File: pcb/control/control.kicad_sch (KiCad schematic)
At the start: 2 parts, among them U1 PicoW, U2 SN65HVD230DR

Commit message: Working on control PCB more
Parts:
- added C1: 4.7uF, symbol Device:C
- added C2: 10uF, symbol Device:C
- added C3: 100nF, symbol Device:C
- added CR1: PESD1CAN_215, pesd:SOT23_PESD1_NEX, symbol pesd:PESD1CAN_215
- added J1: Barrel_Jack_MountingPin, Connector_BarrelJack:BarrelJack_CUI_PJ-102AH_Horizontal, symbol Connector:Barrel_Jack_MountingPin
- added R1, R2: 60Ω, symbol Device:R
- added R3: R, symbol Device:R
- added R4: 100KΩ, symbol Device:R
- added R5, R6, R7: PTA4543, POT_PTA4543, symbol pta4543:PTA4543-2015DPA103
- added U3: FDN340P, fdn340p:SOT-23_ONS, symbol fdn340p:FDN340P
- added U4: DMG2305UX-7, SOT-23_DIO, symbol dmg2305ux:DMG2305UX-7
- U1: footprint RPi_PicoW:RPi_Pico_SMD_TH -> pico:RPi_PicoW_SMD_TH
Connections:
- net GND: now reaches U1.13 (GND)
- net GND: now also U1.18 (GND), U1.23 (GND), U1.28 (GND), U1.3 (GND), U1.33 (AGND), U1.38 (GND), U1.42 (GND), U1.8 (GND), U2.2 (GND), C1.2, C2.2, C3.2, CR1.3, J1.2, R3.2, R5.3, R6.3, R7.3
- net LED_ON: now reaches U1.14 (GPIO10)
- net LED_R: now reaches U1.15 (GPIO11)
- net LED_G: now reaches U1.16 (GPIO12)
- net LED_B: now reaches U1.19 (GPIO14)
- net LED_WIFI: now reaches U1.20 (GPIO15)
- net CAN_TX: now reaches U1.21 (GPIO16)
- net CAN_TX: now also U2.1 (D)
- net CAN_RX: now reaches U1.22 (GPIO17)
- net CAN_RX: now also U2.4 (R)
- net CAN_ENL: now reaches U1.29 (GPIO22)
- net CAN_ENL: now also R4.2, U3.1
- net POT_R: now reaches U1.31 (GPIO26_ADC0)
- net POT_R: now also R5.2
- net POT_G: now reaches U1.32 (GPIO27_ADC1)
- net POT_G: now also R6.2
- net POT_B: now reaches U1.34 (GPIO28_ADC2)
- net POT_B: now also R7.2
- net VSYS: now reaches U1.39 (VSYS)
- net VSYS: now also U2.3 (VCC), C2.1, C3.1, R4.1, R5.1, R6.1, R7.1, U3.2, U4.2
- net VBUS: now reaches U1.40 (VBUS)
- net VBUS: now also U4.1
- net CAN_VREF: now reaches U2.5 (VREF)
- net CAN_VREF: now also C1.1, R1.2, R2.1
- net CANL: now reaches U2.6 (CANL)
- net CANL: now also CR1.2, R2.2
- net CANH: now reaches U2.7 (CANH)
- net CANH: now also CR1.1, R1.1
- net CAN_RS: now reaches U2.8 (RS)
- net CAN_RS: now also R3.1, U3.3
- new net VBARREL: J1.1, U4.3
- no-connect marks 0 -> 20
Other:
- note added: "5V Supply"
- note added: "CAN Transceiver"
- note added: "Color Sliders"
- note added: "ESD Protection"
- note added: "Enable Logic"
- note added: "Microcontroller"
- note added: "Power"
- note added: "Split Termination"
- moved on the sheet: U1, U2

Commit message: Schematic finished, working on layout
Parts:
- added D1, D2, D3, D4, D5: LED, LED_THT:LED_D5.0mm, symbol Device:LED
- added J2: Screw_Terminal_01x02, TerminalBlock_TE-Connectivity:TerminalBlock_TE_282834-2_1x02_P2.54mm_Horizontal, symbol Connector:Screw_Terminal_01x02
- added R10, R11, R8, R9: 60Ω, Resistor_SMD:R_1206_3216Metric, symbol Device:R
- added R12: 5Ω, Resistor_SMD:R_0603_1608Metric, symbol Device:R
- added S1: RM103772BCB, rm103772bcb:RM103772BCB, symbol rm103772bcb:RM103772BCB
- added SW1, SW2: OS102011MS2QN1, os102011ms2qn1:SPDT_OS102011_CNK, symbol os102011ms2qn1:OS102011MS2QN1
- C1, C2, C3: footprint (none) -> Capacitor_SMD:C_0603_1608Metric
- R1, R2: footprint (none) -> Resistor_SMD:R_1206_3216Metric
- R3: value R -> 10KΩ; footprint (none) -> Resistor_SMD:R_0603_1608Metric
- R4: footprint (none) -> Resistor_SMD:R_0603_1608Metric
- U4: footprint SOT-23_DIO -> dmg2305ux:SOT-23_DIO
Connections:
- net CANH: now also J2.1 (Pin_1)
- net CANL: now also J2.2 (Pin_2)
- net GND: now also R10.2, R11.2, R12.2, R8.2, R9.2, SW1.3, SW2.3
- net LED_B: now also D5.2 (A)
- net LED_G: now also D4.2 (A)
- net LED_ON: now also D1.2 (A)
- net LED_R: now also D3.2 (A)
- net LED_WIFI: now also D2.2 (A)
- net VSYS: now also S1.8 (C), SW1.1, SW2.1
- net M_LIGHT: now reaches U1.10 (GPIO7)
- net M_LIGHT: now also S1.1
- net M_MUSIC: now reaches U1.11 (GPIO8)
- net M_MUSIC: now also S1.2
- net M_ON: now reaches U1.12 (GPIO9)
- net M_ON: now also S1.3
- net SYS_EN: now reaches U1.6 (GPIO4)
- net SYS_EN: now also SW1.2
- net SYS_WIFI: now reaches U1.7 (GPIO5)
- net SYS_WIFI: now also SW2.2
- new net: D1.1 (K), R8.1
- new net: D4.1 (K), R11.1
- new net: D5.1 (K), R12.1
- new net: D3.1 (K), R10.1
- new net: D2.1 (K), R9.1
- no-connect marks 20 -> 21
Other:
- note added: "B"
- note added: "Enable"
- note added: "G"
- note added: "LEDs"
- note added: "Mode"
- note added: "On"
- note added: "R"
- note added: "Screw Terminal"
- note added: "Switches"
- note added: "WiFi"

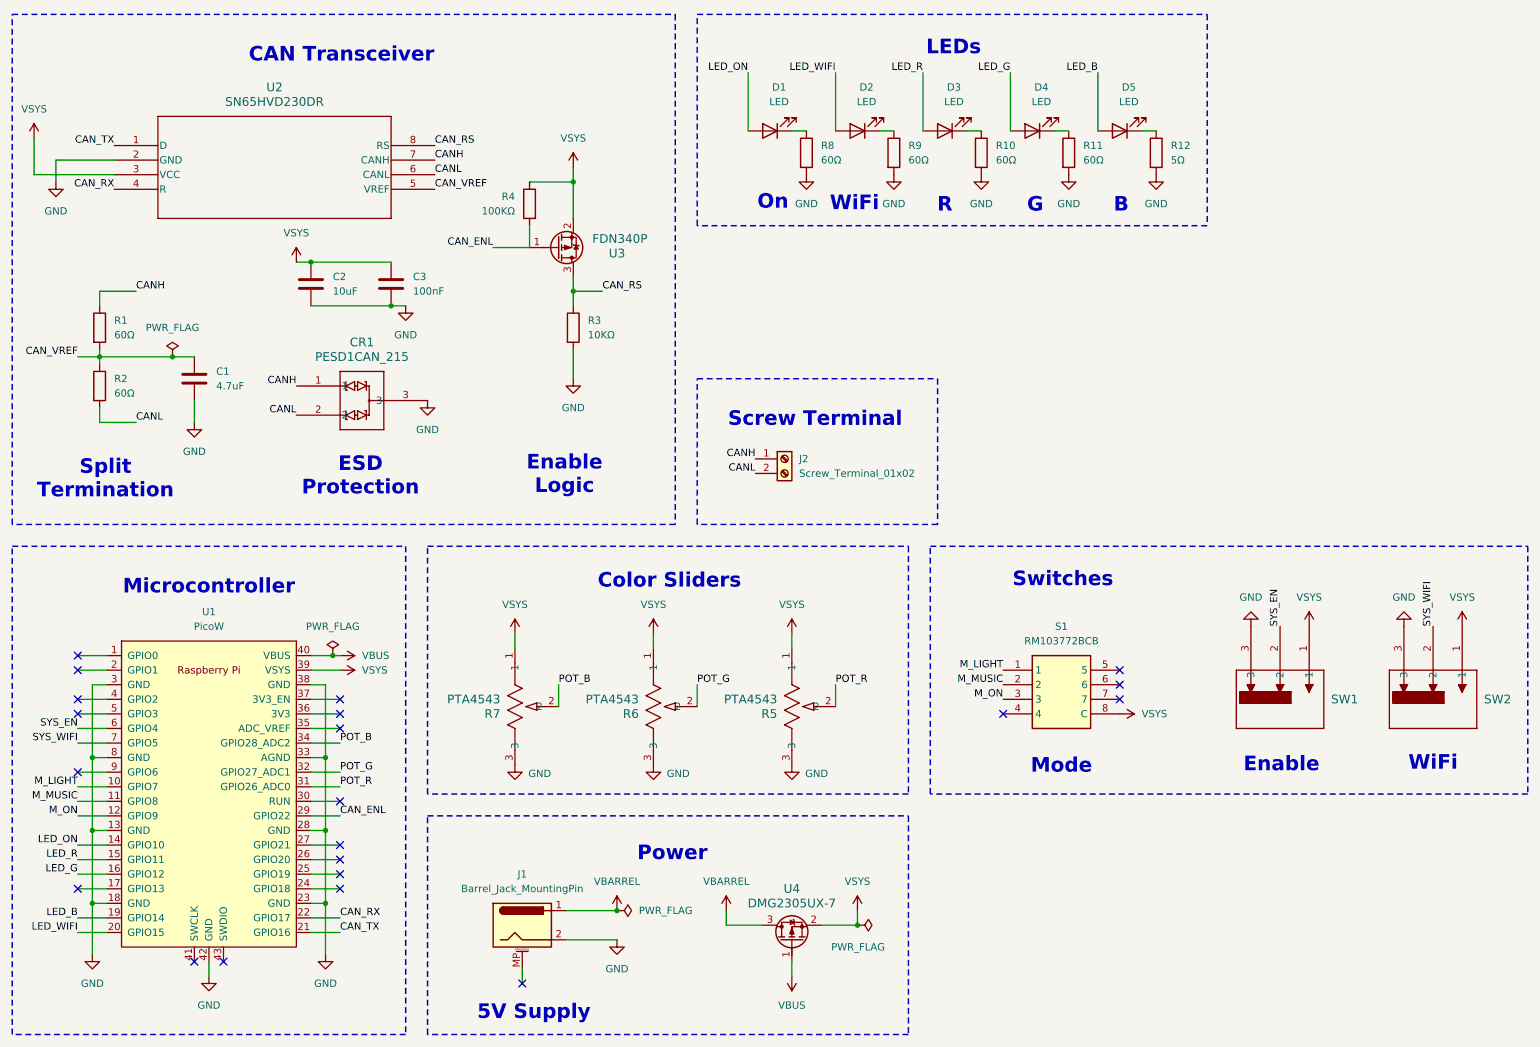
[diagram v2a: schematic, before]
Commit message: Update control schematic
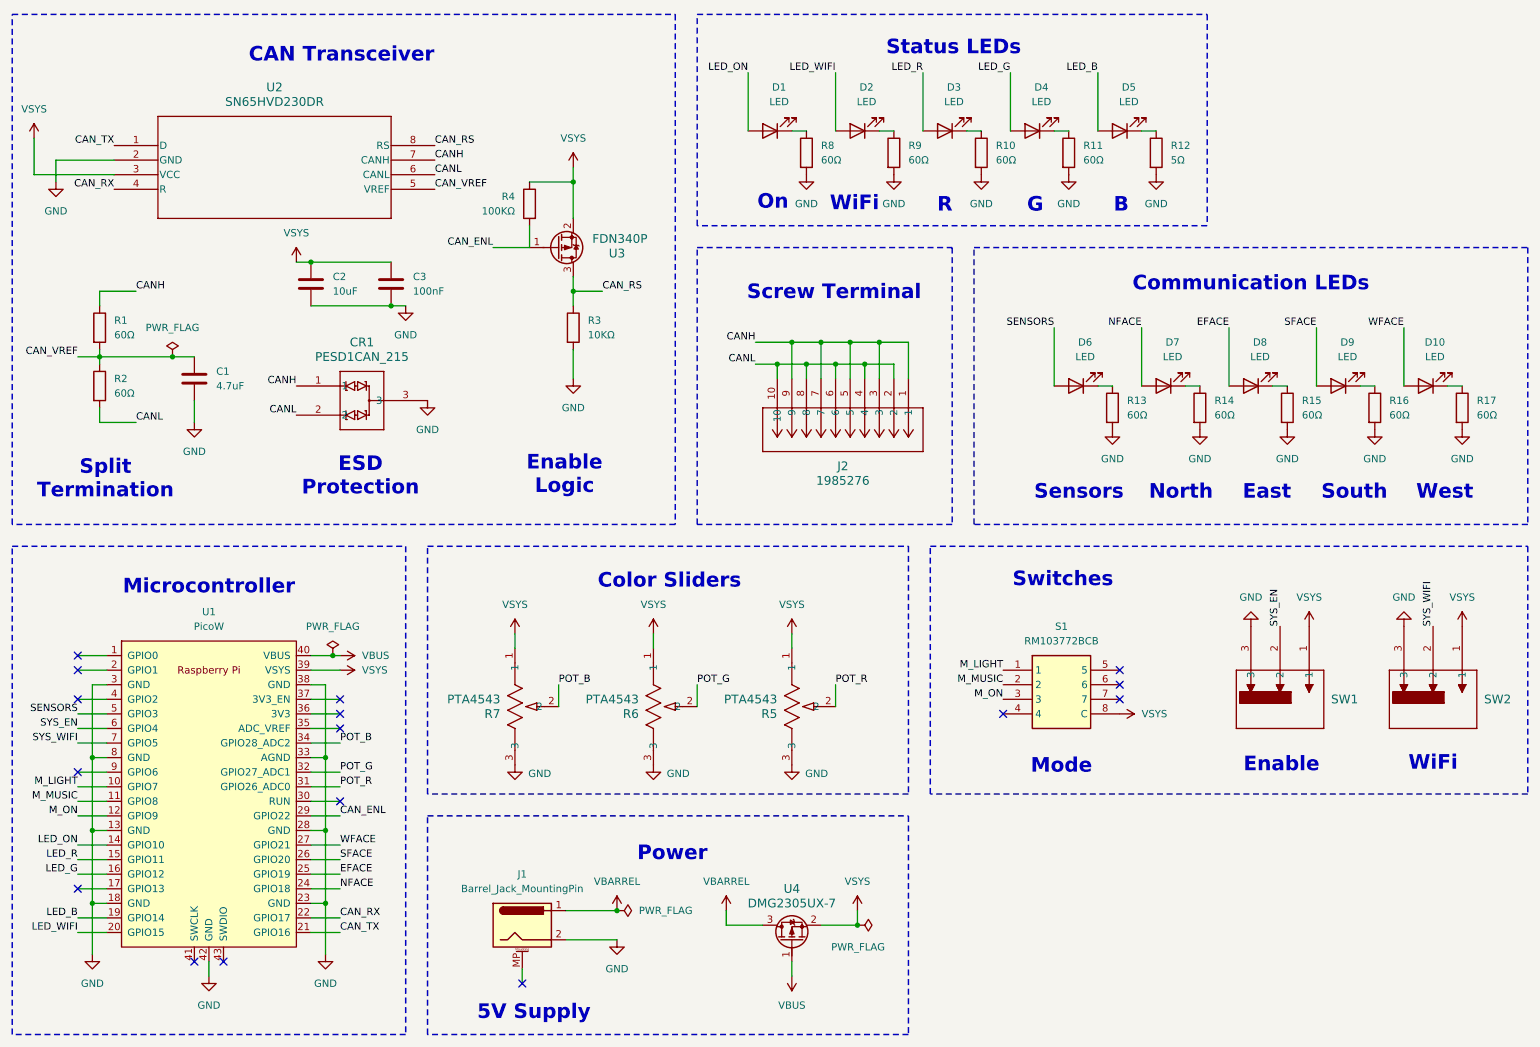
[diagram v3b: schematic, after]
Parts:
- removed J2: Screw_Terminal_01x02, TerminalBlock_TE-Connectivity:TerminalBlock_TE_282834-2_1x02_P2.54mm_Horizontal, symbol Connector:Screw_Terminal_01x02
- added D10, D6, D7, D8, D9: LED, LED_THT:LED_D5.0mm, symbol Device:LED
- added J2: 1985276, CONN_1985276_PXC, symbol 1985276:1985276
- added R13, R14, R15, R16: 60Ω, Resistor_SMD:R_1206_3216Metric, symbol Device:R
- added R17: 60Ω, Resistor_SMD:R_0603_1608Metric, symbol Device:R
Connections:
- net CANH: now also J2.1, J2.3, J2.5, J2.7, J2.9
- net CANL: now also J2.10, J2.2, J2.4, J2.6, J2.8
- net GND: now also R13.2, R14.2, R15.2, R16.2, R17.2
- net NFACE: now reaches U1.24 (GPIO18)
- net NFACE: now also D7.2 (A)
- net EFACE: now reaches U1.25 (GPIO19)
- net EFACE: now also D8.2 (A)
- net SFACE: now reaches U1.26 (GPIO20)
- net SFACE: now also D9.2 (A)
- net WFACE: now reaches U1.27 (GPIO21)
- net WFACE: now also D10.2 (A)
- net SENSORS: now reaches U1.5 (GPIO3)
- net SENSORS: now also D6.2 (A)
- new net: D10.1 (K), R17.1
- new net: D6.1 (K), R13.1
- new net: D9.1 (K), R16.1
- new net: D8.1 (K), R15.1
- new net: D7.1 (K), R14.1
- no-connect marks 21 -> 16
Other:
- note added: "Communication LEDs"
- note added: "East"
- note added: "North"
- note added: "Sensors"
- note added: "South"
- note added: "Status LEDs"
- note added: "West"
- note removed: "LEDs"

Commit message: Control PCB done
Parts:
- removed J2: 1985276, CONN_1985276_PXC, symbol 1985276:1985276
- added J2: 1729092, 1729092:PHOENIX_1729092, symbol 1729092:1729092
- R17: footprint Resistor_SMD:R_0603_1608Metric -> Resistor_SMD:R_1206_3216Metric
- R5, R6, R7: footprint POT_PTA4543 -> pta4543:POT_PTA4543
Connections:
- net CANH: now also CR1.2, J2.1, J2.3, J2.5, J2.7, J2.9; no longer CR1.1
- net CANL: now also CR1.1, J2.10, J2.2, J2.4, J2.6, J2.8; no longer CR1.2
- net NFACE: now also U1.27 (GPIO21); no longer U1.24 (GPIO18)
- net POT_B: now also U1.31 (GPIO26_ADC0); no longer U1.34 (GPIO28_ADC2)
- net POT_R: now also U1.34 (GPIO28_ADC2); no longer U1.31 (GPIO26_ADC0)
- net WFACE: now also U1.24 (GPIO18); no longer U1.27 (GPIO21)

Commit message: PCBs hopefully done
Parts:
- added H1, H2: MountingHole, MountingHole:MountingHole_3.2mm_M3_DIN965_Pad, symbol Mechanical:MountingHole
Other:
- note added: "Mounting"
- moved on the sheet: R5, R6, R7, S1, SW1, SW2

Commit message: Final boards
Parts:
- D1, D10, D2, D3, D4, D5, D6, D7, D8, D9: footprint LED_THT:LED_D5.0mm -> LED_SMD:LED_0603_1608Metric
- R10, R13, R14, R15, R16, R17, R8, R9: value 60Ω -> 750Ω
- R11: value 60Ω -> 325Ω; footprint Resistor_SMD:R_1206_3216Metric -> Resistor_SMD:R_0603_1608Metric
- R12: value 5Ω -> 325Ω
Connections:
- net VSYS: no longer C2.1, C3.1, R4.1, R5.1, R6.1, R7.1, S1.8 (C), SW1.1, SW2.1, U2.3 (VCC), U3.2
- net +3V3: now reaches U1.36 (3V3)
- net +3V3: now also C2.1, C3.1, R4.1, R5.1, R6.1, R7.1, S1.8 (C), SW1.1, SW2.1, U2.3 (VCC), U3.2
- no-connect marks 16 -> 15
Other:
- note removed: "Switches"
- moved on the sheet: S1
